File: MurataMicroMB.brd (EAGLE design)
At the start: 90 x 63 mm, 63 parts, among them CON1 CON_MICROSD_C2395, CON2 WM17143CT-ND, CON3 CON_MIL_10_ARM, CON4 CON_MICROSD_C2395, IC1 NC7SZ00M5XCT-ND, IC2 296-35164-1-ND, IC3 IC_LPC11U3XQFN33, IC4 LDO4_3.3_SOT223, Q1 1253-1168-1-ND, SW1 P-8073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

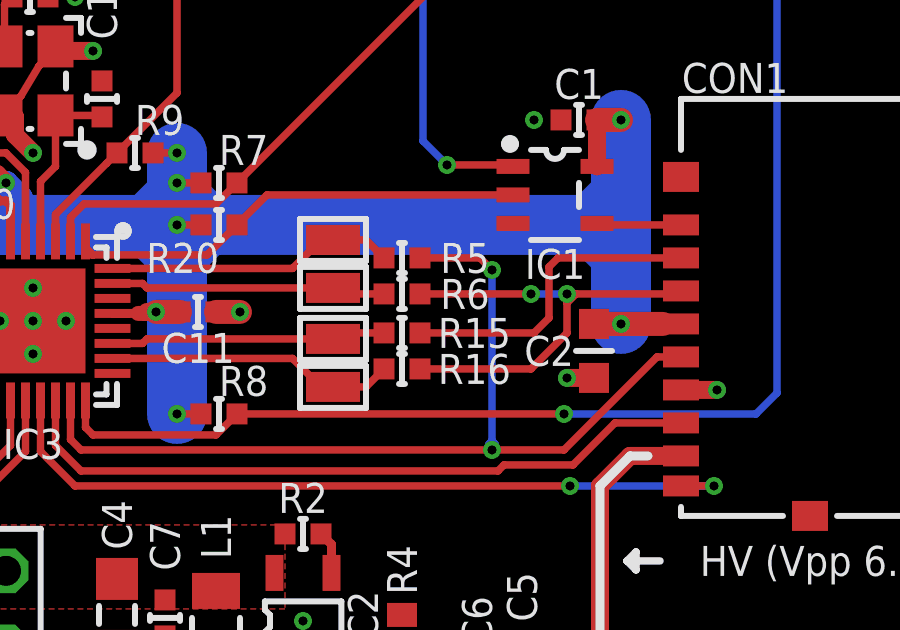
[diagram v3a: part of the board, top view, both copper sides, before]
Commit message: [ MB ] Fiducials renamed; moved TPs
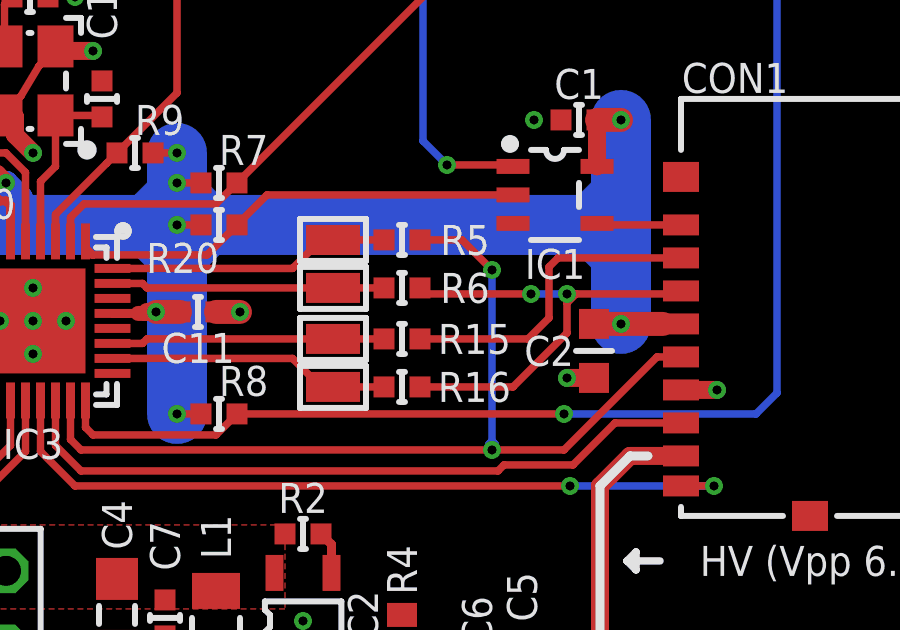
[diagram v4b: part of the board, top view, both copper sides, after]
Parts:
- moved R5 0.60 mm to (54.3, 34.2)
- moved R16 0.60 mm to (54.3, 29.3)
- moved R15 0.20 mm to (54.3, 30.9)
- moved R6 0.20 mm to (54.3, 32.6)
- renumbered TP3 to TP101, TP4 to TP102, TP5 to TP103
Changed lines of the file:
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@@
 <attribute name="DIGIKEY" value="490-3261-1-ND" x="47.5" y="31.8" size="1.778" layer="27" display="off"/>
 </element>
-<element name="R5" library="mylib" package="C0402" value="1k/1005" x="54.3" y="33.6" smashed="yes">
-<attribute name="NAME" x="56.4" y="33.6" size="1" layer="25" font="vector" ratio="20" align="center"/>
-<attribute name="VALUE" x="53.7" y="31.7" size="1" layer="27" font="vector" ratio="20"/>
-<attribute name="AKIZUKI" value="" x="54.3" y="33.6" size="1.778" layer="27" display="off"/>
-<attribute name="MOUSER" value="" x="54.3" y="33.6" size="1.778" layer="27" display="off"/>
-<attribute name="DIGIKEY" value="P1.00KLCT-ND " x="54.3" y="33.6" size="1.778" layer="27" display="off"/>
-</element>
-<element name="R6" library="mylib" package="C0402" value="1k/1005" x="54.3" y="32.4" smashed="yes">
-<attribute name="NAME" x="56.4" y="32.4" size="1" layer="25" font="vector" ratio="20" align="center"/>
-<attribute name="VALUE" x="53.7" y="30.5" size="1" layer="27" font="vector" ratio="20"/>
-<attribute name="AKIZUKI" value="" x="54.3" y="32.4" size="1.778" layer="27" display="off"/>
-<attribute name="MOUSER" value="" x="54.3" y="32.4" size="1.778" layer="27" display="off"/>
-<attribute name="DIGIKEY" value="P1.00KLCT-ND " x="54.3" y="32.4" size="1.778" layer="27" display="off"/>
+<element name="R5" library="mylib" package="C0402" value="1k/1005" x="54.3" y="34.2" smashed="yes">
+<attribute name="NAME" x="56.4" y="34.2" size="1" layer="25" font="vector" ratio="20" align="center"/>
+<attribute name="VALUE" x="53.7" y="32.3" size="1" layer="27" font="vector" ratio="20"/>
+<attribute name="AKIZUKI" value="" x="54.3" y="34.2" size="1.778" layer="27" display="off"/>
+<attribute name="MOUSER" value="" x="54.3" y="34.2" size="1.778" layer="27" display="off"/>
+<attribute name="DIGIKEY" value="P1.00KLCT-ND " x="54.3" y="34.2" size="1.778" layer="27" display="off"/>
+</element>
+<element name="R6" library="mylib" package="C0402" value="1k/1005" x="54.3" y="32.6" smashed="yes">
+<attribute name="NAME" x="56.4" y="32.6" size="1" layer="25" font="vector" ratio="20" align="center"/>
+<attribute name="VALUE" x="53.7" y="30.7" size="1" layer="27" font="vector" ratio="20"/>
+<attribute name="AKIZUKI" value="" x="54.3" y="32.6" size="1.778" layer="27" display="off"/>
+<attribute name="MOUSER" value="" x="54.3" y="32.6" size="1.778" layer="27" display="off"/>
+<attribute name="DIGIKEY" value="P1.00KLCT-ND " x="54.3" y="32.6" size="1.778" layer="27" display="off"/>
 </element>
 <element name="R7" library="mylib" package="C0402" value="10k/1005" x="48.2" y="36.1" smashed="yes">
@@
 <attribute name="VALUE" x="36.8" y="39.7" size="1" layer="27" font="vector" ratio="20" align="center"/>
 </element>
-<element name="R15" library="mylib" package="C0402" value="1k/1005" x="54.3" y="31.1" smashed="yes">
-<attribute name="NAME" x="55.5" y="30.6" size="1" layer="25" font="vector" ratio="20"/>
-<attribute name="VALUE" x="53.7" y="29.2" size="1" layer="27" font="vector" ratio="20"/>
-<attribute name="AKIZUKI" value="" x="54.3" y="31.1" size="1.778" layer="27" display="off"/>
-<attribute name="MOUSER" value="" x="54.3" y="31.1" size="1.778" layer="27" display="off"/>
-<attribute name="DIGIKEY" value="P1.00KLCT-ND " x="54.3" y="31.1" size="1.778" layer="27" display="off"/>
-</element>
-<element name="R16" library="mylib" package="C0402" value="1k/1005" x="54.3" y="29.9" smashed="yes">
-<attribute name="NAME" x="55.5" y="29.4" size="1" layer="25" font="vector" ratio="20"/>
-<attribute name="VALUE" x="53.7" y="28" size="1" layer="27" font="vector" ratio="20"/>
-<attribute name="AKIZUKI" value="" x="54.3" y="29.9" size="1.778" layer="27" display="off"/>
-<attribute name="MOUSER" value="" x="54.3" y="29.9" size="1.778" layer="27" display="off"/>
-<attribute name="DIGIKEY" value="P1.00KLCT-ND " x="54.3" y="29.9" size="1.778" layer="27" display="off"/>
-</element>
-<element name="TP3" library="mylib" package="FIDUCIAL" value="TESTPAD_F" x="15" y="5"/>
-<element name="TP4" library="mylib" package="FIDUCIAL" value="TESTPAD_F" x="70" y="5"/>
-<element name="TP5" library="mylib" package="FIDUCIAL" value="TESTPAD_F" x="15" y="58"/>
+<element name="R15" library="mylib" package="C0402" value="1k/1005" x="54.3" y="30.9" smashed="yes">
+<attribute name="NAME" x="55.5" y="30.4" size="1" layer="25" font="vector" ratio="20"/>
+<attribute name="VALUE" x="53.7" y="29" size="1" layer="27" font="vector" ratio="20"/>
+<attribute name="AKIZUKI" value="" x="54.3" y="30.9" size="1.778" layer="27" display="off"/>
+<attribute name="MOUSER" value="" x="54.3" y="30.9" size="1.778" layer="27" display="off"/>
+<attribute name="DIGIKEY" value="P1.00KLCT-ND " x="54.3" y="30.9" size="1.778" layer="27" display="off"/>
+</element>
+<element name="R16" library="mylib" package="C0402" value="1k/1005" x="54.3" y="29.3" smashed="yes">
+<attribute name="NAME" x="55.5" y="28.8" size="1" layer="25" font="vector" ratio="20"/>
+<attribute name="VALUE" x="53.7" y="27.4" size="1" layer="27" font="vector" ratio="20"/>
+<attribute name="AKIZUKI" value="" x="54.3" y="29.3" size="1.778" layer="27" display="off"/>
+<attribute name="MOUSER" value="" x="54.3" y="29.3" size="1.778" layer="27" display="off"/>
+<attribute name="DIGIKEY" value="P1.00KLCT-ND " x="54.3" y="29.3" size="1.778" layer="27" display="off"/>
+</element>
+<element name="TP101" library="mylib" package="FIDUCIAL" value="TESTPAD_F" x="15" y="5"/>
+<element name="TP102" library="mylib" package="FIDUCIAL" value="TESTPAD_F" x="70" y="5"/>
+<element name="TP103" library="mylib" package="FIDUCIAL" value="TESTPAD_F" x="15" y="58"/>
 <element name="R17" library="mylib" package="C0402" value="10k/1005" x="34.8" y="36.2" smashed="yes" rot="R270">
 <attribute name="NAME" x="35.3" y="37.4" size="1" layer="25" font="vector" ratio="20" rot="R90"/>
@@
 <wire x1="43.25" y1="27.55" x2="43.25" y2="28.85" width="0.25" layer="1"/>
 <contactref element="R5" pad="2"/>
-<wire x1="54.9" y1="33.6" x2="56.9" y2="33.6" width="0.25" layer="1"/>
-<wire x1="56.9" y1="33.6" x2="57.3" y2="33.2" width="0.25" layer="1"/>
+<wire x1="54.9" y1="34.2" x2="56.3" y2="34.2" width="0.25" layer="1"/>
+<wire x1="56.3" y1="34.2" x2="57.3" y2="33.2" width="0.25" layer="1"/>
 <via x="57.3" y="33.2" extent="1-16" drill="0.3"/>
 <wire x1="57.3" y1="33.2" x2="57.3" y2="27.5" width="0.25" layer="16"/>
@@
 <wire x1="63.1" y1="32.4" x2="60.1" y2="32.4" width="0.25" layer="1"/>
 <wire x1="60.1" y1="32.4" x2="59.8" y2="32.4" width="0.25" layer="1"/>
-<wire x1="54.9" y1="32.4" x2="58.6" y2="32.4" width="0.25" layer="1"/>
+<wire x1="54.9" y1="32.6" x2="55.1" y2="32.4" width="0.25" layer="1"/>
+<wire x1="55.1" y1="32.4" x2="58.6" y2="32.4" width="0.25" layer="1"/>
 <via x="58.6" y="32.4" extent="1-16" drill="0.3"/>
 <wire x1="58.6" y1="32.4" x2="59.8" y2="32.4" width="0.25" layer="16"/>
@@
 <wire x1="60.1" y1="32.4" x2="59.8" y2="32.1" width="0.25" layer="1"/>
 <contactref element="R16" pad="2"/>
-<wire x1="54.9" y1="29.9" x2="58.6" y2="29.9" width="0.25" layer="1"/>
-<wire x1="58.6" y1="29.9" x2="59.8" y2="31.1" width="0.25" layer="1"/>
+<wire x1="54.9" y1="29.3" x2="58" y2="29.3" width="0.25" layer="1"/>
+<wire x1="58" y1="29.3" x2="59.8" y2="31.1" width="0.25" layer="1"/>
 </signal>
 <signal name="!CS!">
@@
 <wire x1="59.2" y1="33.3" x2="59.5" y2="33.6" width="0.25" layer="1"/>
 <contactref element="R15" pad="2"/>
-<wire x1="54.9" y1="31.1" x2="58.7" y2="31.1" width="0.25" layer="1"/>
-<wire x1="58.7" y1="31.1" x2="59.2" y2="31.6" width="0.25" layer="1"/>
+<wire x1="54.9" y1="30.9" x2="58.5" y2="30.9" width="0.25" layer="1"/>
+<wire x1="58.5" y1="30.9" x2="59.2" y2="31.6" width="0.25" layer="1"/>
 </signal>
 <signal name="VPP">
@@
 <wire x1="45.65" y1="32.75" x2="45.8" y2="32.6" width="0.25" layer="1"/>
 <wire x1="45.8" y1="32.6" x2="52" y2="32.6" width="0.25" layer="1"/>
-<wire x1="53.7" y1="32.4" x2="52.2" y2="32.4" width="0.25" layer="1"/>
-<wire x1="52.2" y1="32.4" x2="52" y2="32.6" width="0.25" layer="1"/>
+<wire x1="53.7" y1="32.6" x2="52" y2="32.6" width="0.25" layer="1"/>
 </signal>
 <signal name="N$9">
@@
 <wire x1="51.6" y1="34.2" x2="50.65" y2="33.25" width="0.25" layer="1"/>
 <wire x1="44.65" y1="33.25" x2="50.65" y2="33.25" width="0.25" layer="1"/>
-<wire x1="52" y1="34.2" x2="53.1" y2="34.2" width="0.25" layer="1"/>
-<wire x1="53.1" y1="34.2" x2="53.7" y2="33.6" width="0.25" layer="1"/>
+<wire x1="52" y1="34.2" x2="53.7" y2="34.2" width="0.25" layer="1"/>
 </signal>
 <signal name="ISP">
@@
 <wire x1="52" y1="29.3" x2="51.6" y2="29.3" width="0.25" layer="1"/>
 <wire x1="51.6" y1="29.3" x2="50.65" y2="30.25" width="0.25" layer="1"/>
-<wire x1="52" y1="29.3" x2="53.1" y2="29.3" width="0.25" layer="1"/>
-<wire x1="53.1" y1="29.3" x2="53.7" y2="29.9" width="0.25" layer="1"/>
+<wire x1="52" y1="29.3" x2="53.7" y2="29.3" width="0.25" layer="1"/>
 </signal>
 <signal name="N$18">
@@
 <wire x1="45.8" y1="30.9" x2="45.65" y2="30.75" width="0.25" layer="1"/>
 <wire x1="44.65" y1="30.75" x2="45.65" y2="30.75" width="0.25" layer="1"/>
-<wire x1="53.7" y1="31.1" x2="52.2" y2="31.1" width="0.25" layer="1"/>
-<wire x1="52.2" y1="31.1" x2="52" y2="30.9" width="0.25" layer="1"/>
+<wire x1="53.7" y1="30.9" x2="52" y2="30.9" width="0.25" layer="1"/>
 </signal>
 <signal name="TGT_RST">

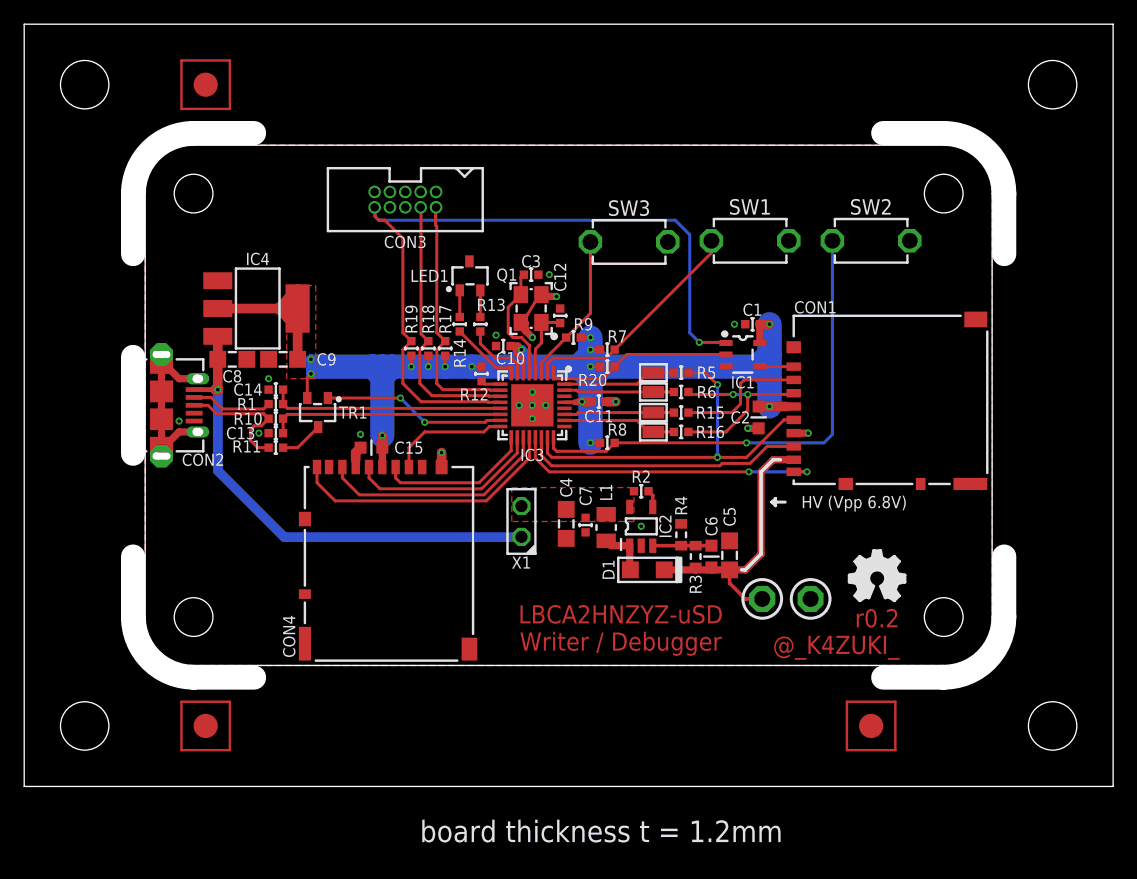
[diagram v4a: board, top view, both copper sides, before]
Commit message: [ MB ] update package of LED1; add TP_4020; update package of IC2
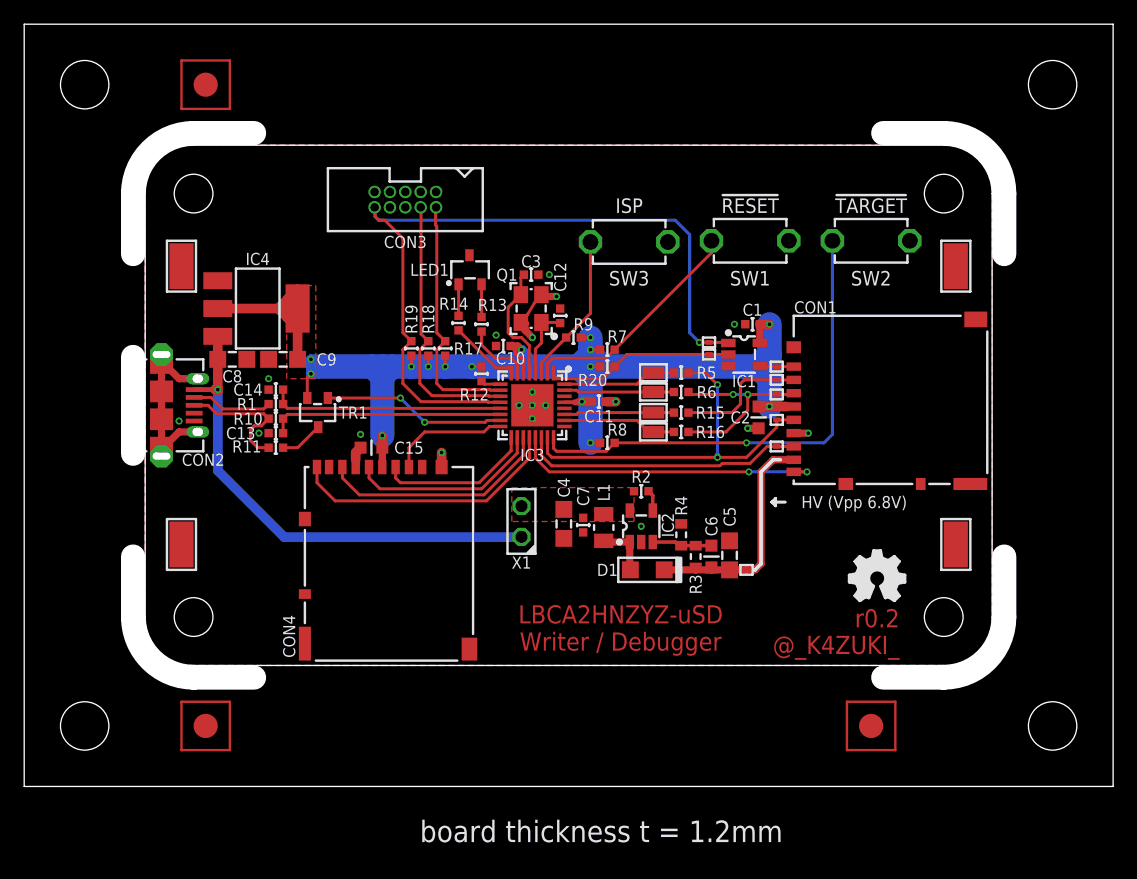
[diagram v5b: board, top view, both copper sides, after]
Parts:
- added TP10, TP11, TP12, TP5: (no value), mylib:TP06RECT
- added TP13, TP14, TP15, TP16: (no value), mylib:TP_4020
- added TP3, TP4: TESTPAD_1608, mylib:TP_1608
- CON3: value CON_MIL_10_ARM -> (none)
- D1: value DIODE_SMALL -> 40V2A
- IC1: value NC7SZ00M5XCT-ND -> (none); device 74xx-little-us_local:SOT23-5 -> mylib:SOT95P280X145-5N
- IC2: value 296-35164-1-ND -> (none); device mylib:IC_05_0.95_50MIL -> mylib:SOT95P280X145-5N
- IC3: value IC_LPC11U3XQFN33 -> IC_LPC11U35_QFN33_5X5
- L1: value INDUCTOR_4.7U_2016 -> 4.7u/2016
- LED1: value 754-1633-1-ND -> RD/GR; device mylib:SOT95P300X140-3N -> mylib:SOT105P300X130-3N
- Q1: value 1253-1168-1-ND -> 12M/3225
- TP101, TP102, TP103: value TESTPAD_F -> (none)
- TP6, TP7: value TESTPAD_1608 -> (none); device mylib:TP_1608 -> mylib:TP06RECT
- TP8, TP9: value TPPAD1-13 -> (none); device testpad_local:P1-13 -> mylib:TP06RECT
- TR1: value I-4269 -> (none)
- U$1: value ICON_OSHW -> (none)
- moved TP8 14.8 mm to (62.2, 30.3), turned to 90 degrees
- moved TP9 12.9 mm to (62.2, 28.1), turned to 90 degrees
- moved TP7 10.4 mm to (62.2, 32.4), turned to 90 degrees
- moved TP6 10.2 mm to (62.2, 33.6), turned to 90 degrees
- moved LED1 0.50 mm to (36.8, 42.7)
- moved L1 0.20 mm to (47.9, 21.4)
- moved C4 0.20 mm to (44.6, 21.7)
- moved C7 0.20 mm to (46.2, 21.6)
- moved R14 0.14 mm to (35.9, 38.3)
- moved IC1 0.10 mm to (59.5, 35.7), turned to 0 degrees
- moved R13 0.10 mm to (37.8, 38.2)
- turned IC2 to 90 degrees
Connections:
- removed net N$3: CON1.DAT2, IC1.4
- new net RESET: CON1.DAT2, IC1.4, TP5.TP
- net !CS!: now also TP6.TP
- net GND: now also TP13.TP, TP14.TP, TP15.TP, TP16.TP; no longer TP9.TP
- net MISO: now also TP9.TP
- net MOSI: now also TP7.TP
- net N$6: now also TP3.TP; no longer TP6.TP
- net N$9: now also TP4.TP; no longer TP7.TP
- net NSRST: now also TP10.TP
- net SCK: now also TP8.TP
- net TGT_RST: now also TP11.TP
- net VPP: now also TP12.TP; no longer TP8.TP
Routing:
- net VPP: track 23.2 -> 19.3 mm
- net N$3: track 2.85 -> 0.00 mm
- net RESET: track 0.00 -> 2.82 mm
- net N$15: track 2.20 -> 2.70 mm
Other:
- board text added: "!RESET!"
- board text added: "!TARGET!"
- board text added: "ISP"
